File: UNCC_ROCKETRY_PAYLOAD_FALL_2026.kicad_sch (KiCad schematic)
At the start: 0 parts

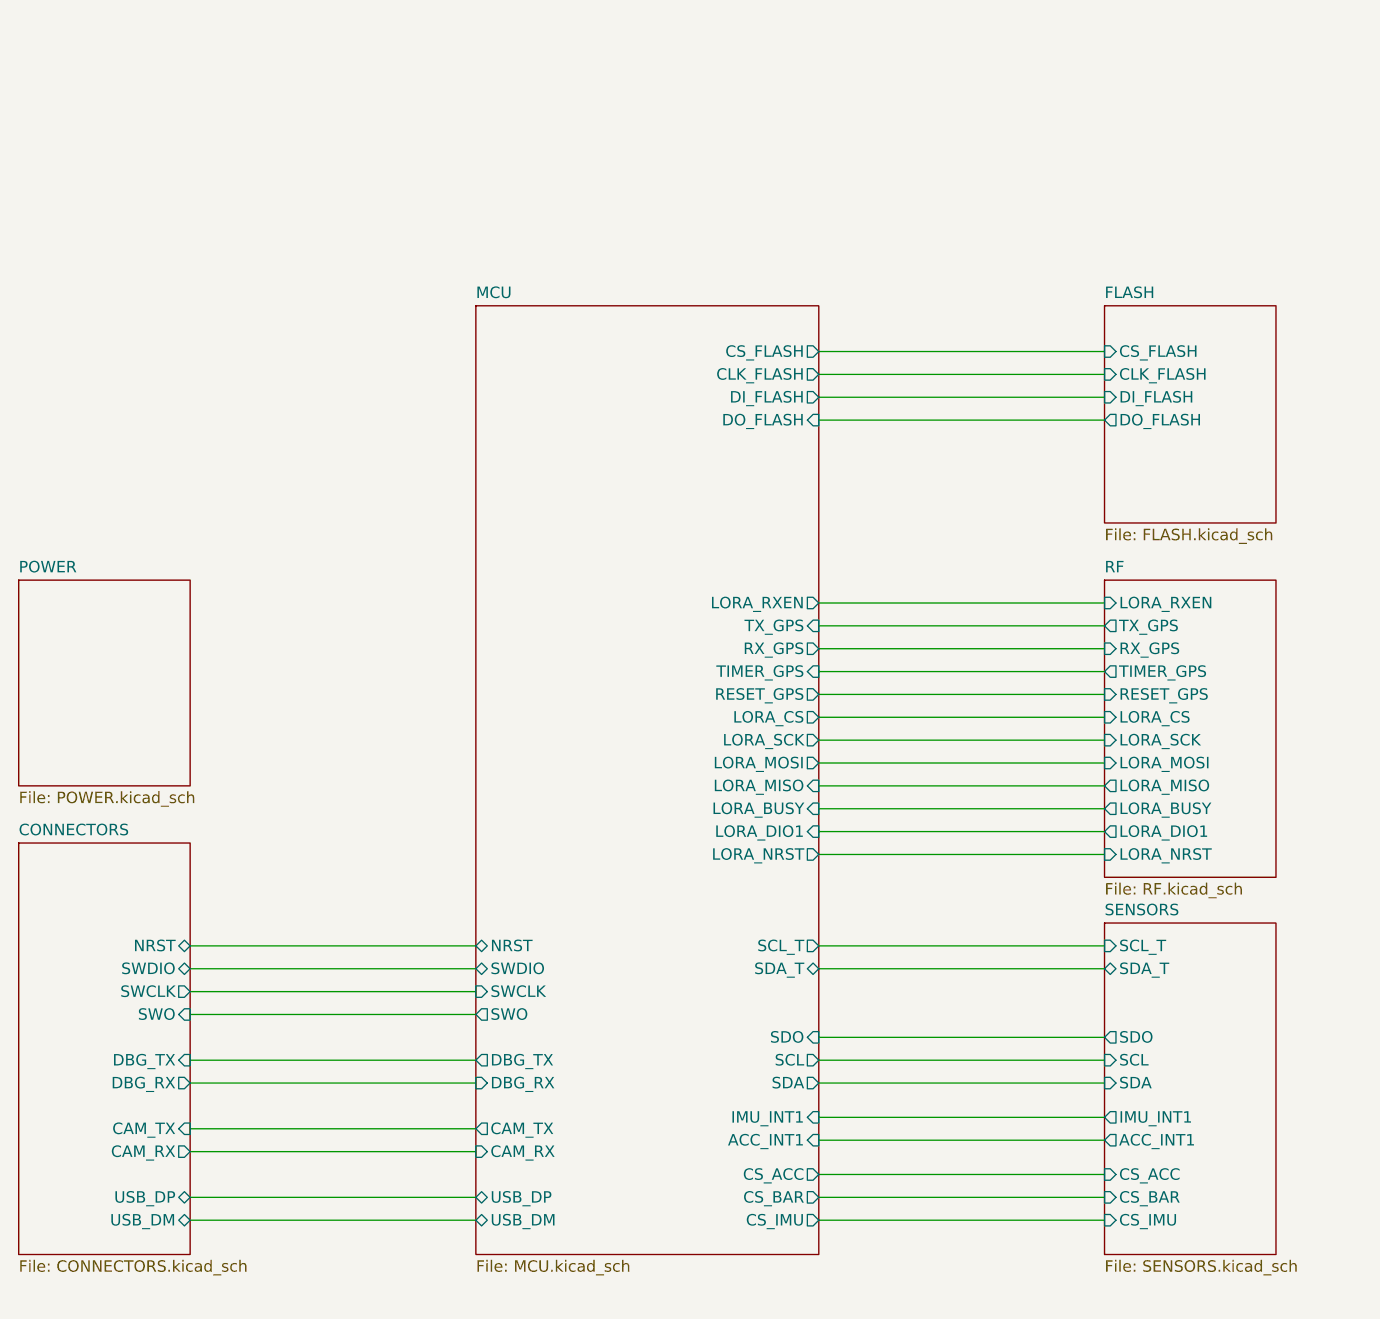
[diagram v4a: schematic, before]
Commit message: Battery protection, camera switch, 64MB flash, ERC clean
- Fuse + TVS on battery input, camera load switch (TPS22917)
- Flash to W25Q512JVFIQ (SOIC-16), hand-solder passive footprints
- Power LED, title blocks, U5 footprint, PWR/NC flags (0 ERC)
- Regenerated schematic PDF
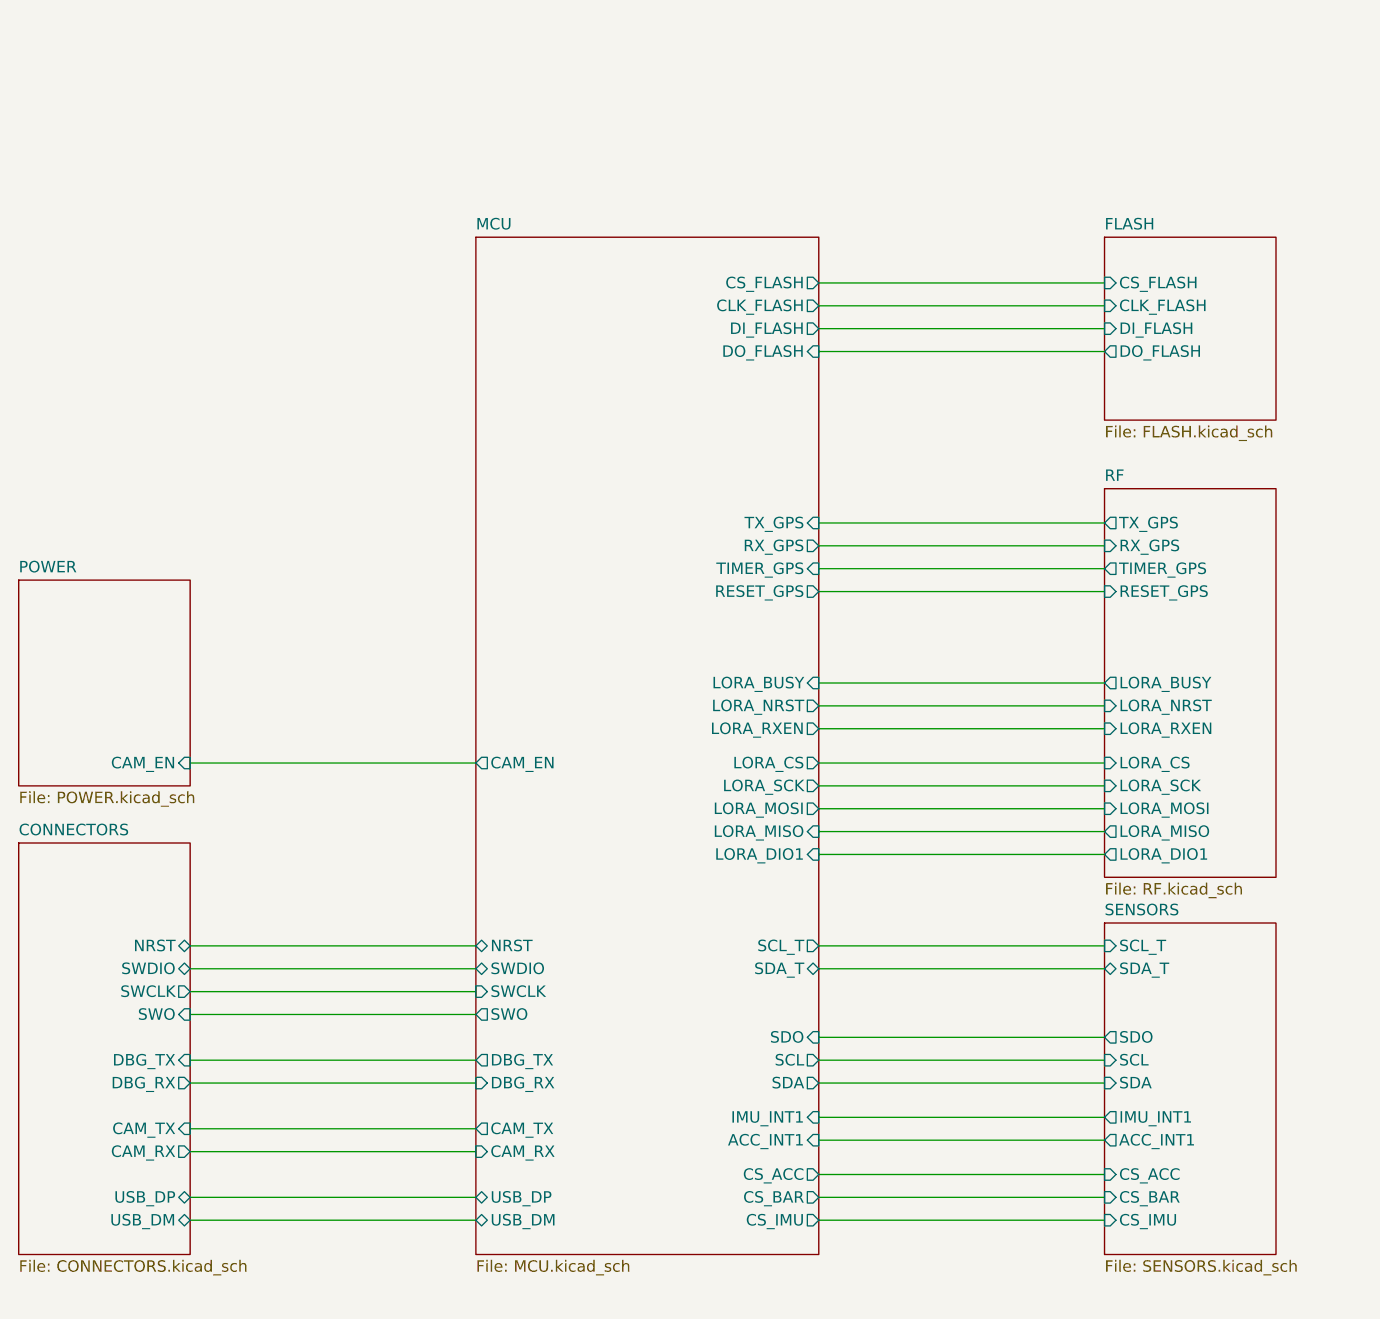
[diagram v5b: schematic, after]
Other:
- sheet MCU ports: added CAM_EN; removed none
- sheet POWER ports: added CAM_EN; removed none
- title: (none) -> UNCC Rocketry Payload, Fall 2026

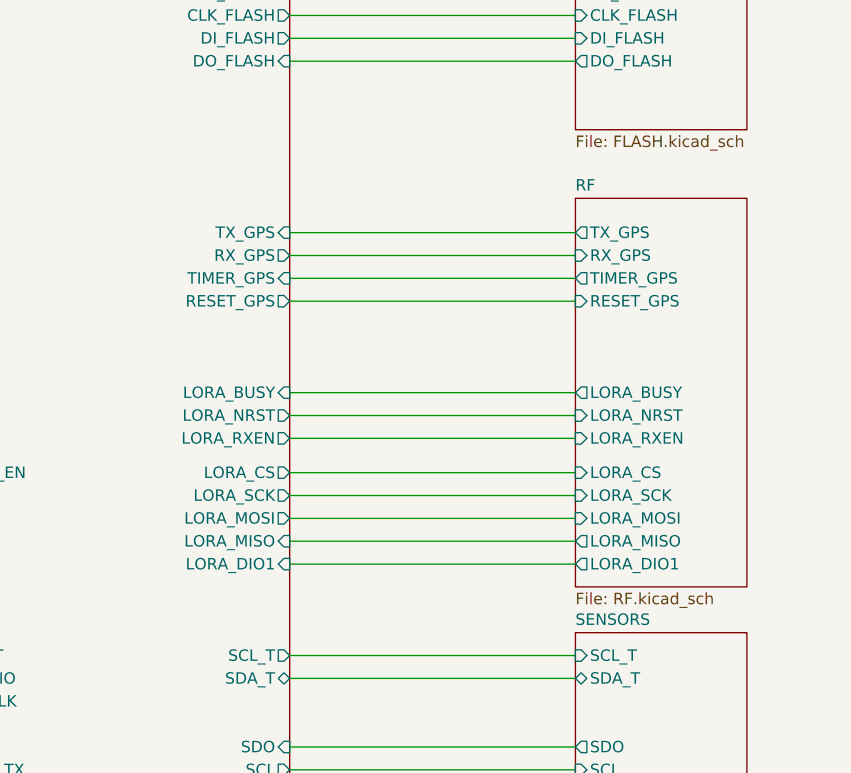
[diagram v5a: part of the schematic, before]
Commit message: updated firmware to fix altitude bug also added mangometer support, updated GUI to have slider for time
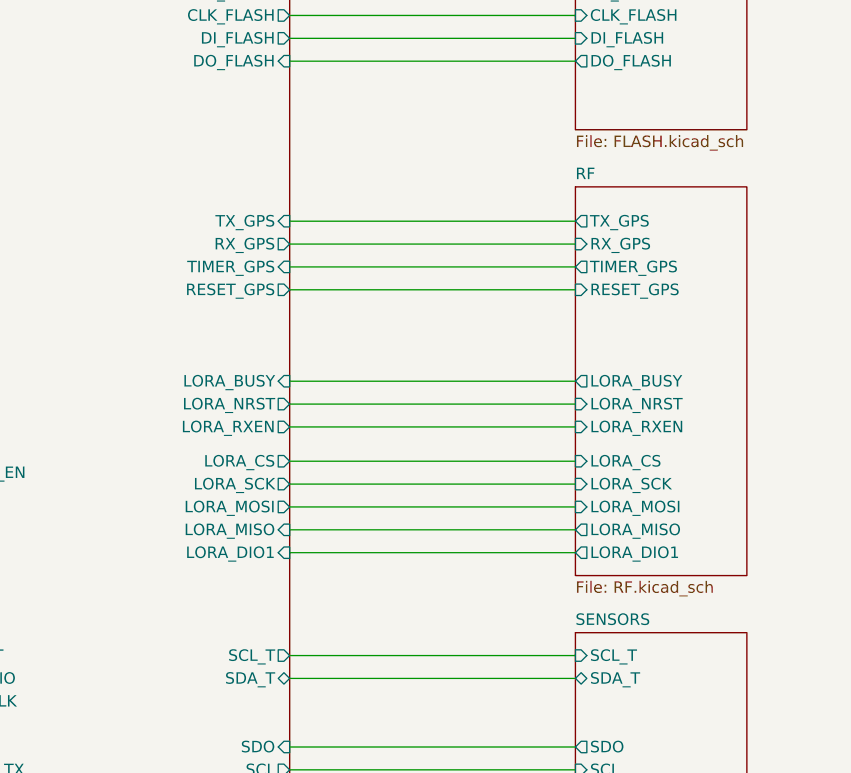
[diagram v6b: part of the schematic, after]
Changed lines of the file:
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@@
 	(wire
 		(pts
-			(xy 158.75 104.14) (xy 190.5 104.14)
+			(xy 158.75 102.87) (xy 190.5 102.87)
 		)
 		(stroke
@@
 	(wire
 		(pts
-			(xy 158.75 109.22) (xy 190.5 109.22)
+			(xy 158.75 107.95) (xy 190.5 107.95)
 		)
 		(stroke
@@
 	(wire
 		(pts
-			(xy 158.75 80.01) (xy 190.5 80.01)
+			(xy 158.75 78.74) (xy 190.5 78.74)
 		)
 		(stroke
@@
 	(wire
 		(pts
-			(xy 158.75 111.76) (xy 190.5 111.76)
+			(xy 158.75 110.49) (xy 190.5 110.49)
 		)
 		(stroke
@@
 	(wire
 		(pts
-			(xy 158.75 101.6) (xy 190.5 101.6)
+			(xy 158.75 100.33) (xy 190.5 100.33)
 		)
 		(stroke
@@
 	(wire
 		(pts
-			(xy 158.75 106.68) (xy 190.5 106.68)
+			(xy 158.75 105.41) (xy 190.5 105.41)
 		)
 		(stroke
@@
 	(wire
 		(pts
-			(xy 158.75 97.79) (xy 190.5 97.79)
+			(xy 158.75 96.52) (xy 190.5 96.52)
 		)
 		(stroke
@@
 	(wire
 		(pts
-			(xy 158.75 82.55) (xy 190.5 82.55)
-		)
-		(stroke
-			(width 0)
-			(type default)
-		)
-	)
-	(wire
-		(pts
-			(xy 158.75 95.25) (xy 190.5 95.25)
-		)
-		(stroke
-			(width 0)
-			(type default)
-		)
-	)
-	(wire
-		(pts
-			(xy 158.75 74.93) (xy 190.5 74.93)
-		)
-		(stroke
-			(width 0)
-			(type default)
-		)
-	)
-	(wire
-		(pts
-			(xy 158.75 92.71) (xy 190.5 92.71)
+			(xy 158.75 81.28) (xy 190.5 81.28)
+		)
+		(stroke
+			(width 0)
+			(type default)
+		)
+	)
+	(wire
+		(pts
+			(xy 158.75 93.98) (xy 190.5 93.98)
+		)
+		(stroke
+			(width 0)
+			(type default)
+		)
+	)
+	(wire
+		(pts
+			(xy 158.75 73.66) (xy 190.5 73.66)
+		)
+		(stroke
+			(width 0)
+			(type default)
+		)
+	)
+	(wire
+		(pts
+			(xy 158.75 91.44) (xy 190.5 91.44)
 		)
 		(stroke
@@
 	(wire
 		(pts
-			(xy 158.75 77.47) (xy 190.5 77.47)
+			(xy 158.75 76.2) (xy 190.5 76.2)
 		)
 		(stroke
@@
 		)
 		(pin "TX_GPS" input
-			(at 158.75 74.93 0)
+			(at 158.75 73.66 0)
 			(effects
 				(font
@@
 		)
 		(pin "RX_GPS" output
-			(at 158.75 77.47 0)
+			(at 158.75 76.2 0)
 			(effects
 				(font
@@
 		)
 		(pin "TIMER_GPS" input
-			(at 158.75 80.01 0)
+			(at 158.75 78.74 0)
 			(effects
 				(font
@@
 		)
 		(pin "RESET_GPS" output
-			(at 158.75 82.55 0)
+			(at 158.75 81.28 0)
 			(effects
 				(font
@@
 		)
 		(pin "LORA_RXEN" output
-			(at 158.75 97.79 0)
+			(at 158.75 96.52 0)
 			(effects
 				(font
@@
 		)
 		(pin "LORA_CS" output
-			(at 158.75 101.6 0)
+			(at 158.75 100.33 0)
 			(effects
 				(font
@@
 		)
 		(pin "LORA_SCK" output
-			(at 158.75 104.14 0)
+			(at 158.75 102.87 0)
 			(effects
 				(font
@@
 		)
 		(pin "LORA_MOSI" output
-			(at 158.75 106.68 0)
+			(at 158.75 105.41 0)
 			(effects
 				(font
@@
 		)
 		(pin "LORA_MISO" input
-			(at 158.75 109.22 0)
+			(at 158.75 107.95 0)
 			(effects
 				(font
@@
 		)
 		(pin "LORA_BUSY" input
-			(at 158.75 92.71 0)
+			(at 158.75 91.44 0)
 			(effects
 				(font
@@
 		)
 		(pin "LORA_DIO1" input
-			(at 158.75 111.76 0)
+			(at 158.75 110.49 0)
 			(effects
 				(font
@@
 		)
 		(pin "LORA_NRST" output
-			(at 158.75 95.25 0)
+			(at 158.75 93.98 0)
 			(effects
 				(font
@@
 	)
 	(sheet
-		(at 190.5 71.12)
+		(at 190.5 69.85)
 		(size 19.05 43.18)
 		(exclude_from_sim no)
@@
 		)
 		(property "Sheetname" "RF"
-			(at 190.5 70.4084 0)
+			(at 190.5 69.1384 0)
 			(show_name no)
 			(do_not_autoplace no)
@@
 		)
 		(property "Sheetfile" "RF.kicad_sch"
-			(at 190.5 114.8846 0)
+			(at 190.5 113.6146 0)
 			(show_name no)
 			(do_not_autoplace no)
@@
 		)
 		(pin "TX_GPS" output
-			(at 190.5 74.93 180)
+			(at 190.5 73.66 180)
 			(effects
 				(font
@@
 		)
 		(pin "RX_GPS" input
-			(at 190.5 77.47 180)
+			(at 190.5 76.2 180)
 			(effects
 				(font
@@
 		)
 		(pin "TIMER_GPS" output
-			(at 190.5 80.01 180)
+			(at 190.5 78.74 180)
 			(effects
 				(font
@@
 		)
 		(pin "RESET_GPS" input
-			(at 190.5 82.55 180)
+			(at 190.5 81.28 180)
 			(effects
 				(font
@@
 		)
 		(pin "LORA_RXEN" input
-			(at 190.5 97.79 180)
+			(at 190.5 96.52 180)
 			(effects
 				(font
@@
 		)
 		(pin "LORA_CS" input
-			(at 190.5 101.6 180)
+			(at 190.5 100.33 180)
 			(effects
 				(font
@@
 		)
 		(pin "LORA_SCK" input
-			(at 190.5 104.14 180)
+			(at 190.5 102.87 180)
 			(effects
 				(font
@@
 		)
 		(pin "LORA_MOSI" input
-			(at 190.5 106.68 180)
+			(at 190.5 105.41 180)
 			(effects
 				(font
@@
 		)
 		(pin "LORA_MISO" output
-			(at 190.5 109.22 180)
+			(at 190.5 107.95 180)
 			(effects
 				(font
@@
 		)
 		(pin "LORA_BUSY" output
-			(at 190.5 92.71 180)
+			(at 190.5 91.44 180)
 			(effects
 				(font
@@
 		)
 		(pin "LORA_DIO1" output
-			(at 190.5 111.76 180)
+			(at 190.5 110.49 180)
 			(effects
 				(font
@@
 		)
 		(pin "LORA_NRST" input
-			(at 190.5 95.25 180)
-			(effects
-				(font
+			(at 190.5 93.98 180)
+			(effects
+				(font

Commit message: started layout
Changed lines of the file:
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@@
 		)
 		(pin "TX_GPS" output
-			(at 190.5 73.66 180)
+			(at 209.55 73.66 0)
 			(effects
 				(font
 					(size 1.27 1.27)
 				)
-				(justify left)
+				(justify right)
 			)
 		)
 		(pin "RX_GPS" input
-			(at 190.5 76.2 180)
+			(at 209.55 76.2 0)
 			(effects
 				(font
 					(size 1.27 1.27)
 				)
-				(justify left)
+				(justify right)
 			)
 		)
 		(pin "TIMER_GPS" output
-			(at 190.5 78.74 180)
+			(at 209.55 78.74 0)
 			(effects
 				(font
 					(size 1.27 1.27)
 				)
-				(justify left)
+				(justify right)
 			)
 		)
 		(pin "RESET_GPS" input
-			(at 190.5 81.28 180)
+			(at 209.55 81.28 0)
 			(effects
 				(font
 					(size 1.27 1.27)
 				)
-				(justify left)
+				(justify right)
 			)
 		)
 		(pin "LORA_RXEN" input
-			(at 190.5 96.52 180)
+			(at 209.55 96.52 0)
 			(effects
 				(font
 					(size 1.27 1.27)
 				)
-				(justify left)
+				(justify right)
 			)
 		)
 		(pin "LORA_CS" input
-			(at 190.5 100.33 180)
+			(at 209.55 100.33 0)
 			(effects
 				(font
 					(size 1.27 1.27)
 				)
-				(justify left)
+				(justify right)
 			)
 		)
 		(pin "LORA_SCK" input
-			(at 190.5 102.87 180)
+			(at 209.55 102.87 0)
 			(effects
 				(font
 					(size 1.27 1.27)
 				)
-				(justify left)
+				(justify right)
 			)
 		)
 		(pin "LORA_MOSI" input
-			(at 190.5 105.41 180)
+			(at 209.55 105.41 0)
 			(effects
 				(font
 					(size 1.27 1.27)
 				)
-				(justify left)
+				(justify right)
 			)
 		)
 		(pin "LORA_MISO" output
-			(at 190.5 107.95 180)
+			(at 209.55 107.95 0)
 			(effects
 				(font
 					(size 1.27 1.27)
 				)
-				(justify left)
+				(justify right)
 			)
 		)
 		(pin "LORA_BUSY" output
-			(at 190.5 91.44 180)
+			(at 209.55 91.44 0)
 			(effects
 				(font
 					(size 1.27 1.27)
 				)
-				(justify left)
+				(justify right)
 			)
 		)
 		(pin "LORA_DIO1" output
-			(at 190.5 110.49 180)
+			(at 209.55 110.49 0)
 			(effects
 				(font
 					(size 1.27 1.27)
 				)
-				(justify left)
+				(justify right)
 			)
 		)
 		(pin "LORA_NRST" input
-			(at 190.5 93.98 180)
+			(at 209.55 93.98 0)
 			(effects
 				(font
 					(size 1.27 1.27)
 				)
-				(justify left)
+				(justify right)
 			)
 		)

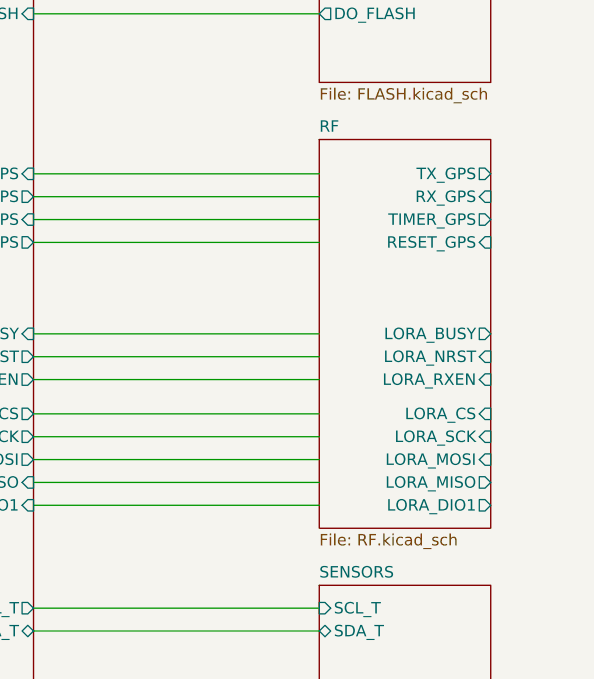
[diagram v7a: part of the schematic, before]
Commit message: layed out components, no routing
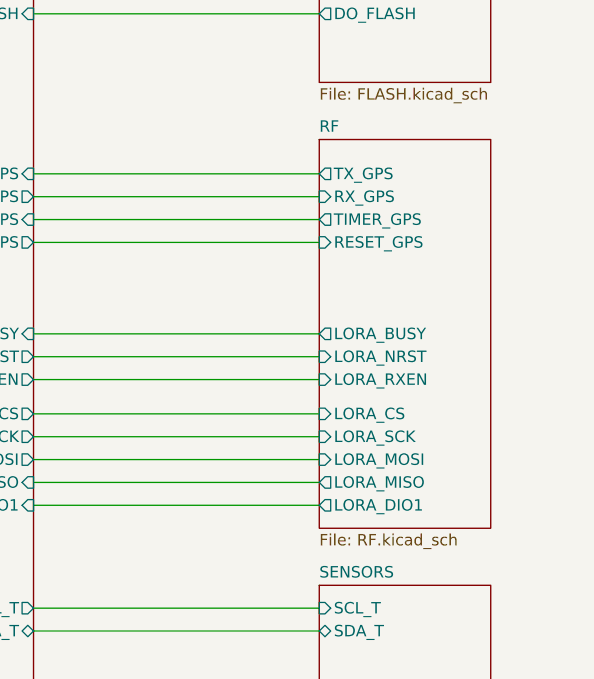
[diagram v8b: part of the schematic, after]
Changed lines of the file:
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@@
 		)
 		(pin "TX_GPS" output
-			(at 209.55 73.66 0)
+			(at 190.5 73.66 180)
 			(effects
 				(font
 					(size 1.27 1.27)
 				)
-				(justify right)
+				(justify left)
 			)
 		)
 		(pin "RX_GPS" input
-			(at 209.55 76.2 0)
+			(at 190.5 76.2 180)
 			(effects
 				(font
 					(size 1.27 1.27)
 				)
-				(justify right)
+				(justify left)
 			)
 		)
 		(pin "TIMER_GPS" output
-			(at 209.55 78.74 0)
+			(at 190.5 78.74 180)
 			(effects
 				(font
 					(size 1.27 1.27)
 				)
-				(justify right)
+				(justify left)
 			)
 		)
 		(pin "RESET_GPS" input
-			(at 209.55 81.28 0)
+			(at 190.5 81.28 180)
 			(effects
 				(font
 					(size 1.27 1.27)
 				)
-				(justify right)
+				(justify left)
 			)
 		)
 		(pin "LORA_RXEN" input
-			(at 209.55 96.52 0)
+			(at 190.5 96.52 180)
 			(effects
 				(font
 					(size 1.27 1.27)
 				)
-				(justify right)
+				(justify left)
 			)
 		)
 		(pin "LORA_CS" input
-			(at 209.55 100.33 0)
+			(at 190.5 100.33 180)
 			(effects
 				(font
 					(size 1.27 1.27)
 				)
-				(justify right)
+				(justify left)
 			)
 		)
 		(pin "LORA_SCK" input
-			(at 209.55 102.87 0)
+			(at 190.5 102.87 180)
 			(effects
 				(font
 					(size 1.27 1.27)
 				)
-				(justify right)
+				(justify left)
 			)
 		)
 		(pin "LORA_MOSI" input
-			(at 209.55 105.41 0)
+			(at 190.5 105.41 180)
 			(effects
 				(font
 					(size 1.27 1.27)
 				)
-				(justify right)
+				(justify left)
 			)
 		)
 		(pin "LORA_MISO" output
-			(at 209.55 107.95 0)
+			(at 190.5 107.95 180)
 			(effects
 				(font
 					(size 1.27 1.27)
 				)
-				(justify right)
+				(justify left)
 			)
 		)
 		(pin "LORA_BUSY" output
-			(at 209.55 91.44 0)
+			(at 190.5 91.44 180)
 			(effects
 				(font
 					(size 1.27 1.27)
 				)
-				(justify right)
+				(justify left)
 			)
 		)
 		(pin "LORA_DIO1" output
-			(at 209.55 110.49 0)
+			(at 190.5 110.49 180)
 			(effects
 				(font
 					(size 1.27 1.27)
 				)
-				(justify right)
+				(justify left)
 			)
 		)
 		(pin "LORA_NRST" input
-			(at 209.55 93.98 0)
+			(at 190.5 93.98 180)
 			(effects
 				(font
 					(size 1.27 1.27)
 				)
-				(justify right)
+				(justify left)
 			)
 		)
